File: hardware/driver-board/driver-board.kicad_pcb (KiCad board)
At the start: 4 copper layers, 111.8 x 83.8 mm, 0 parts

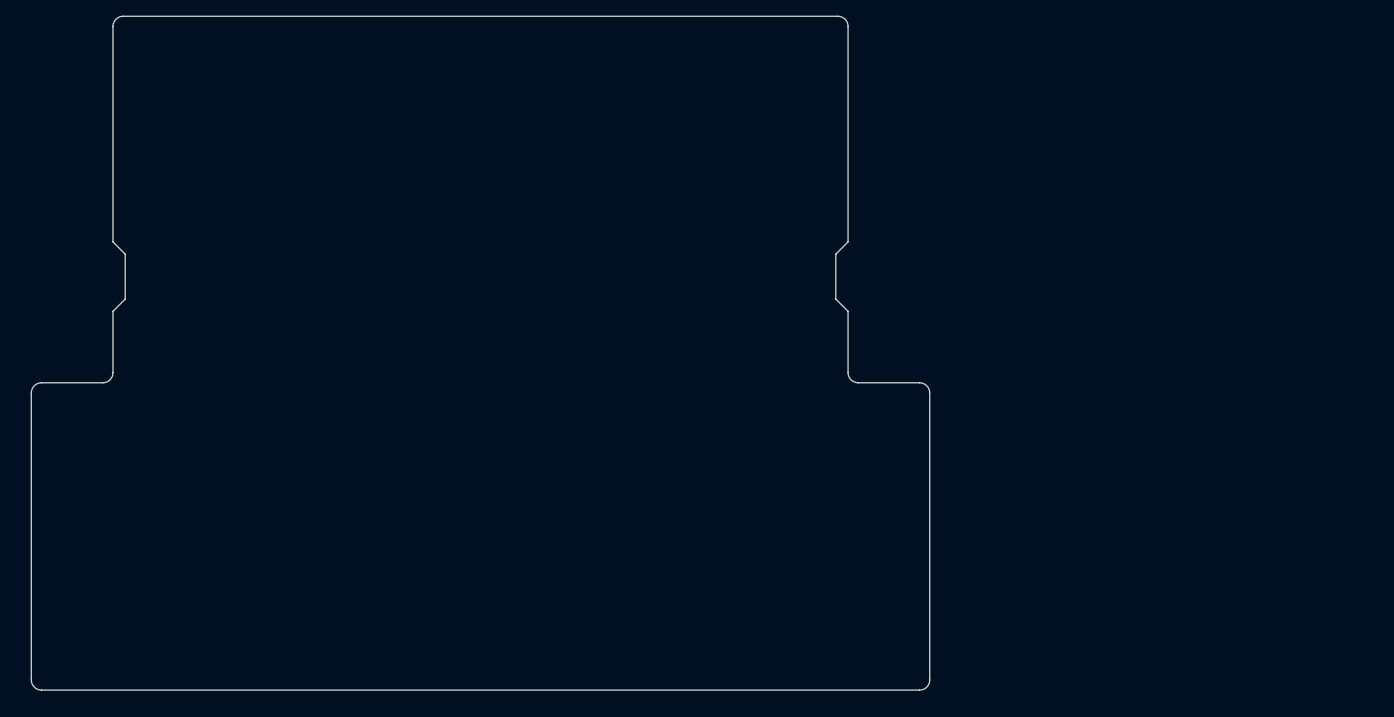
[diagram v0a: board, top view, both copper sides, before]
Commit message: Complete Romi-compatible board placement and power switching
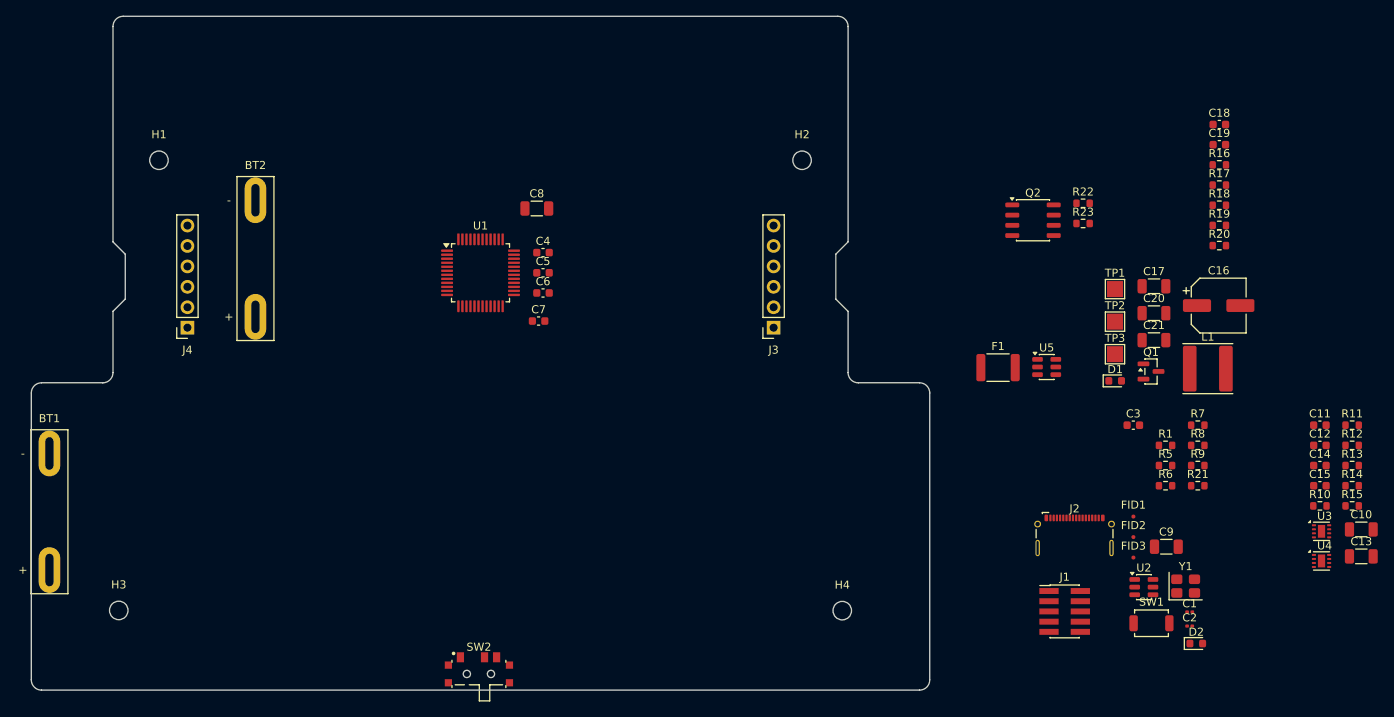
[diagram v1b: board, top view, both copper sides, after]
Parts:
- added BT1: BATT (4xAA), CustomParts:Romi_Chassis_BatteryContactPair_2Slot_14_50mm, F.Cu at (46.4, 119.7)
- added BT2: BATT (2xAA), CustomParts:Romi_Chassis_BatteryContactPair_2Slot_14_50mm, F.Cu at (72.0, 88.2)
- added C1: 10p, Capacitor_SMD:C_0201_0603Metric, F.Cu at (188.2, 132.2)
- added C10: 10u, Capacitor_SMD:C_1206_3216Metric, F.Cu at (209.6, 121.9)
- added C11: 100n, Capacitor_SMD:C_0603_1608Metric, F.Cu at (204.4, 109.0)
- added C12: 100n, Capacitor_SMD:C_0603_1608Metric, F.Cu at (204.4, 111.5)
- added C13: 10u, Capacitor_SMD:C_1206_3216Metric, F.Cu at (209.6, 125.3)
- added C14: 100n, Capacitor_SMD:C_0603_1608Metric, F.Cu at (204.4, 114.0)
- added C15: 100n, Capacitor_SMD:C_0603_1608Metric, F.Cu at (204.4, 116.5)
- added C16: 220u, Capacitor_SMD:CP_Elec_6.3x7.7, F.Cu at (191.8, 94.1)
- added C17: 10u, Capacitor_SMD:C_1206_3216Metric, F.Cu at (183.8, 91.7)
- added C18: 0.1u, Capacitor_SMD:C_0603_1608Metric, F.Cu at (191.9, 71.6)
- added C19: 0.1u, Capacitor_SMD:C_0603_1608Metric, F.Cu at (191.9, 74.1)
- added C2: 10p, Capacitor_SMD:C_0201_0603Metric, F.Cu at (188.2, 133.9)
- added C20: 22u, Capacitor_SMD:C_1206_3216Metric, F.Cu at (183.8, 95.0)
- added C21: 22u, Capacitor_SMD:C_1206_3216Metric, F.Cu at (183.8, 98.4)
- added C3: 100n, Capacitor_SMD:C_0603_1608Metric, F.Cu at (181.2, 109.0)
- added C4: 100n, Capacitor_SMD:C_0603_1608Metric, F.Cu at (107.8, 87.5)
- added C5: 100n, Capacitor_SMD:C_0603_1608Metric, F.Cu at (107.8, 90.0)
- added C6: 100n, Capacitor_SMD:C_0603_1608Metric, F.Cu at (107.8, 92.5)
- added C7: 100n, Capacitor_SMD:C_0603_1608Metric, F.Cu at (107.2, 96.0)
- added C8: 10u, Capacitor_SMD:C_1206_3216Metric, F.Cu at (107.0, 82.0)
- added C9: 10u, Capacitor_SMD:C_1206_3216Metric, F.Cu at (185.3, 124.1)
- added D1: PWR_ON_LED, LED_SMD:LED_0603_1608Metric, F.Cu at (178.9, 103.4)
- added D2: STATUS, LED_SMD:LED_0603_1608Metric, F.Cu at (189.0, 136.1)
- added F1: PTC_2.6A_16V, Fuse:Fuse_1812_4532Metric, F.Cu at (164.4, 101.8)
- added FID1: Fiducial, Fiducial:Fiducial_0.5mm_Mask1mm, F.Cu at (181.2, 120.3)
- added FID2: Fiducial, Fiducial:Fiducial_0.5mm_Mask1mm, F.Cu at (181.2, 122.9)
- added FID3: Fiducial, Fiducial:Fiducial_0.5mm_Mask1mm, F.Cu at (181.2, 125.4)
- added H1: MountingHole, CustomParts:MountingHole_2.3mm_2-56, F.Cu at (60.0, 76.0)
- added H2: MountingHole, CustomParts:MountingHole_2.3mm_2-56, F.Cu at (140.0, 76.0)
- added H3: MountingHole, CustomParts:MountingHole_2.3mm_2-56, F.Cu at (55.0, 132.0)
- added H4: MountingHole, CustomParts:MountingHole_2.3mm_2-56, F.Cu at (145.0, 132.0)
- added J1: Conn_ARM_JTAG_SWD_10, Connector_PinHeader_1.27mm:PinHeader_2x05_P1.27mm_Vertical_SMD, F.Cu at (172.7, 132.1)
- added J2: USB_C_Receptacle_USB2.0_16P, Connector_USB:USB_C_Receptacle_G-Switch_GT-USB-7025, F.Cu at (173.9, 123.9)
- added J3: CONN_MOTOR_R, Connector_PinSocket_2.54mm:PinSocket_1x06_P2.54mm_Vertical, F.Cu at (136.5, 96.8)
- added J4: CONN_MOTOR_L, Connector_PinSocket_2.54mm:PinSocket_1x06_P2.54mm_Vertical, F.Cu at (63.5, 96.8)
- added L1: 5.6u, Inductor_SMD:L_Sunlord_SWPA6045S, F.Cu at (190.5, 101.9)
- added Q1: AO3401A, Package_TO_SOT_SMD:SOT-23, F.Cu at (183.4, 102.3)
- added Q2: AO4407A, CustomParts:AO4407A_SO-8_GSD, F.Cu at (168.7, 83.5)
- added R1: 10k, Resistor_SMD:R_0603_1608Metric, F.Cu at (185.2, 111.5)
- added R10: 10k, Resistor_SMD:R_0603_1608Metric, F.Cu at (204.4, 119.0)
- added R11: 10k, Resistor_SMD:R_0603_1608Metric, F.Cu at (208.4, 109.0)
- added R12: 100k, Resistor_SMD:R_0603_1608Metric, F.Cu at (208.4, 111.5)
- added R13: 100k, Resistor_SMD:R_0603_1608Metric, F.Cu at (208.4, 114.0)
- added R14: 10k, Resistor_SMD:R_0603_1608Metric, F.Cu at (208.4, 116.5)
- added R15: 10k, Resistor_SMD:R_0603_1608Metric, F.Cu at (208.4, 119.0)
- added R16: 100k, Resistor_SMD:R_0603_1608Metric, F.Cu at (191.9, 76.6)
- added R17: 33k, Resistor_SMD:R_0603_1608Metric, F.Cu at (191.9, 79.1)
- added R18: 100k, Resistor_SMD:R_0603_1608Metric, F.Cu at (191.9, 81.6)
- added R19: 22.1k, Resistor_SMD:R_0603_1608Metric, F.Cu at (191.9, 84.1)
- added R20: 1k, Resistor_SMD:R_0603_1608Metric, F.Cu at (191.9, 86.6)
- added R21: 1k, Resistor_SMD:R_0603_1608Metric, F.Cu at (189.2, 116.5)
- added R22: 100k, Resistor_SMD:R_0603_1608Metric, F.Cu at (175.0, 81.4)
- added R23: 1k, Resistor_SMD:R_0603_1608Metric, F.Cu at (175.0, 83.9)
- added R5: 1k5, Resistor_SMD:R_0603_1608Metric, F.Cu at (185.2, 114.0)
- added R6: 5k1, Resistor_SMD:R_0603_1608Metric, F.Cu at (185.2, 116.5)
- added R7: 5k1, Resistor_SMD:R_0603_1608Metric, F.Cu at (189.2, 109.0)
- added R8: 22, Resistor_SMD:R_0603_1608Metric, F.Cu at (189.2, 111.5)
- added R9: 22, Resistor_SMD:R_0603_1608Metric, F.Cu at (189.2, 114.0)
- added SW1: SW_Push, Button_Switch_SMD:SW_SPST_TS-1088-xR020, F.Cu at (183.5, 133.6)
- added SW2: SK-3296S-01-L2, CustomParts:SW_SPDT_RightAngle_XKB_SK-3296S-01-L2, F.Cu at (99.8, 139.9)
- added TP1: TP_3V3, TestPoint:TestPoint_Pad_2.0x2.0mm, F.Cu at (178.9, 92.0)
- added TP2: TP_GND, TestPoint:TestPoint_Pad_2.0x2.0mm, F.Cu at (178.9, 96.1)
- added TP3: TV_BAT, TestPoint:TestPoint_Pad_2.0x2.0mm, F.Cu at (178.9, 100.1)
- added U1: STM32F103CBT6, Package_QFP:LQFP-48_7x7mm_P0.5mm, F.Cu at (100.0, 90.0)
- added U2: USBLC6-2SC6, Package_TO_SOT_SMD:SOT-23-6, F.Cu at (182.5, 129.1)
- added U3: DRV8838, Package_SON:WSON-8-1EP_2x2mm_P0.5mm_EP0.9x1.6mm, F.Cu at (204.6, 122.2)
- added U4: DRV8838, Package_SON:WSON-8-1EP_2x2mm_P0.5mm_EP0.9x1.6mm, F.Cu at (204.6, 125.8)
- added U5: LMR51430XDDCR, Package_TO_SOT_SMD:SOT-23-6, F.Cu at (170.4, 101.7)
- added Y1: 16Mhz, Crystal:Crystal_SMD_3225-4Pin_3.2x2.5mm, F.Cu at (187.7, 129.0)
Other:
- board text added: "BAT1+ ROMI BATTERY SLOT"
- board text added: "BAT1- ROMI BATTERY SLOT"
- board text added: "BAT2+ ROMI BATTERY SLOT"
- board text added: "BAT2- ROMI BATTERY SLOT"

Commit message: Review and harden Rev A driver board
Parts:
- removed FID1, FID2, FID3: Fiducial, Fiducial:Fiducial_0.5mm_Mask1mm
- L1: footprint Inductor_SMD:L_Sunlord_SWPA6045S -> Inductor_SMD:L_APV_ANR8065
- moved C17 158.9 mm to (28.6, 125.8)
- moved C20 158.9 mm to (28.6, 129.1)
- moved C21 158.9 mm to (28.6, 132.4)
- moved R19 158.9 mm to (36.7, 118.2)
- moved TP1 158.9 mm to (23.7, 126.1)
- moved C19 125.6 mm to (78.0, 127.0), turned to 180 degrees
- moved Q1 124.8 mm to (60.0, 121.0), turned to 180 degrees
- moved C18 123.4 mm to (78.0, 119.0), turned to 180 degrees
- moved R18 118.8 mm to (81.0, 124.2), turned to -90 degrees
- moved C16 114.6 mm to (79.0, 114.0), turned to 180 degrees
- moved F1 112.0 mm to (54.0, 121.0)
- moved L1 98.2 mm to (94.0, 120.0), turned to 90 degrees
- moved U5 95.1 mm to (78.0, 124.0)
- moved J2 75.4 mm to (100.0, 139.0)
- moved SW2 34.3 mm to (66.5, 148.0)
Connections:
- net Net-(Q1-D) renamed /Power/VBAT_FUSED
- R21 pad 1: Net-(D2-K) -> +3V3
- R21 pad 2: GND -> Net-(D2-A)
- U1 pad 2: Net-(D2-A) -> Net-(D2-K)

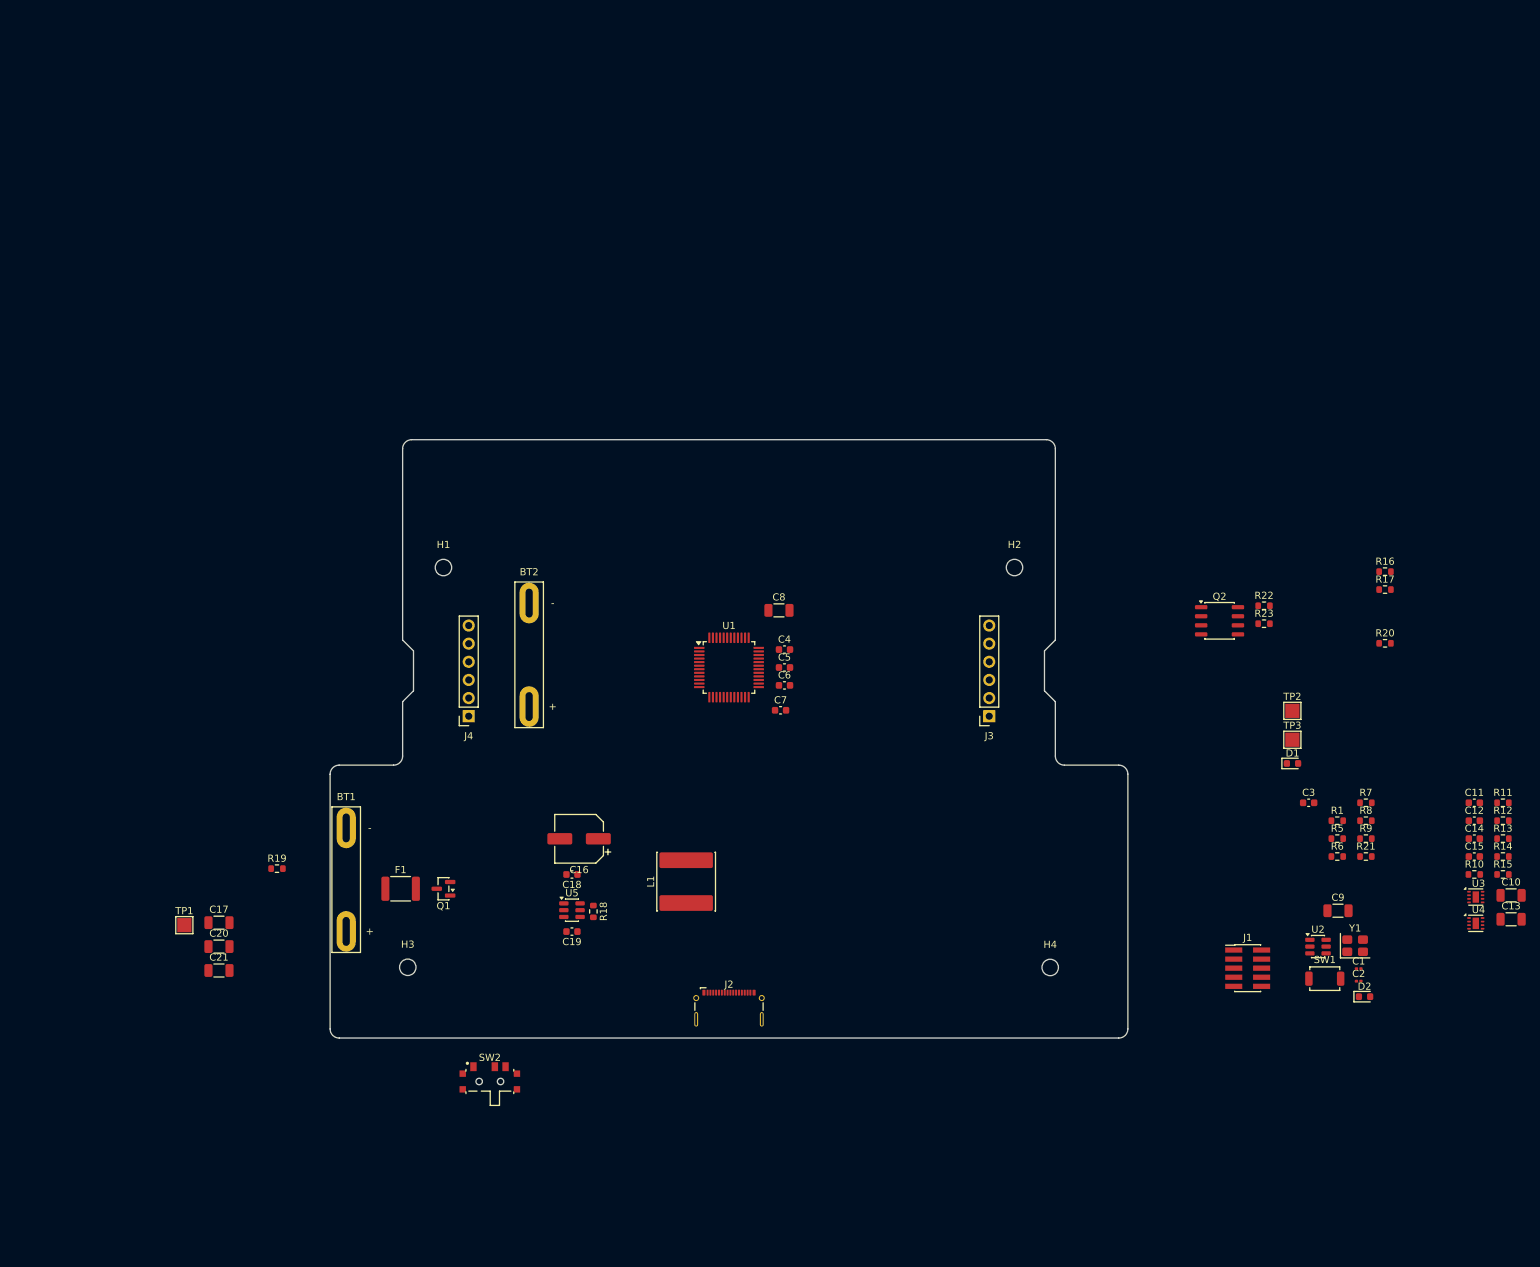
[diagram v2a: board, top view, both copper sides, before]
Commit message: Refine driver board placement and capacitor footprints
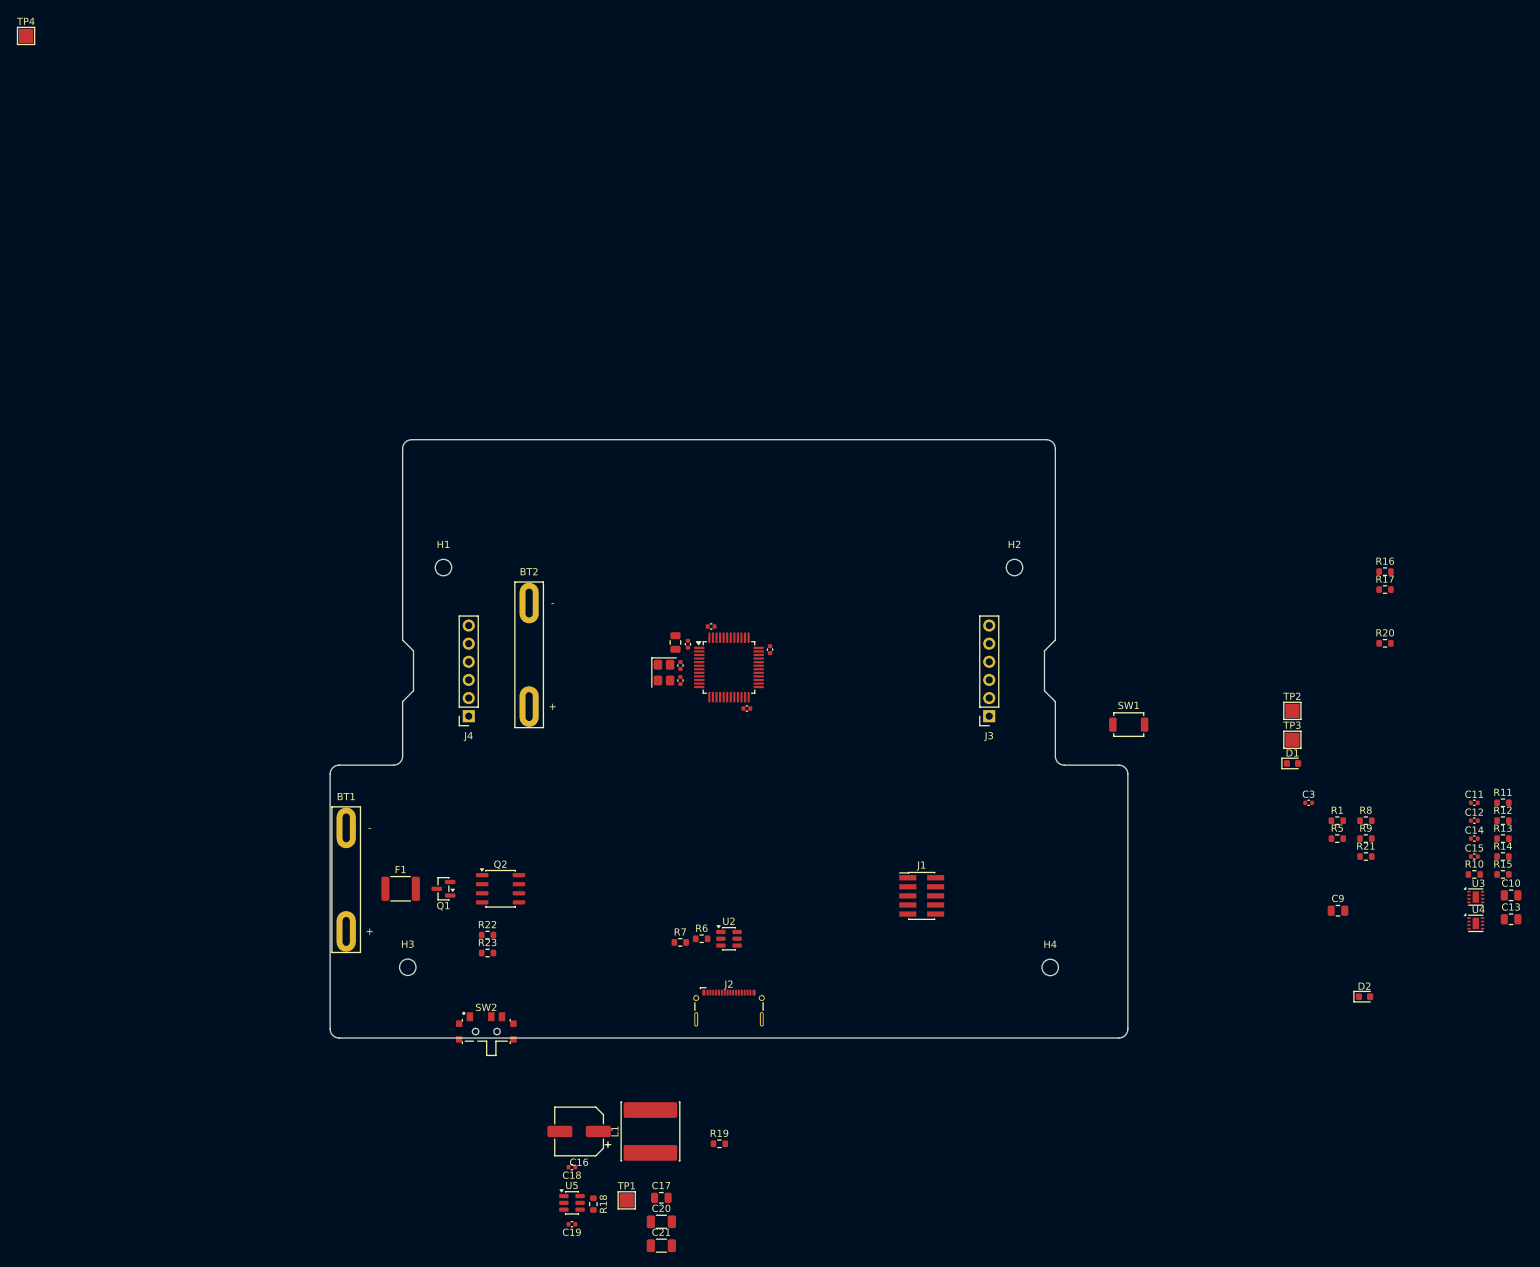
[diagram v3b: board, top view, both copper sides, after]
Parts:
- added TP4: TP_BAT_SW, TestPoint:TestPoint_Pad_2.0x2.0mm, F.Cu at (1.52, 1.52)
- C1, C2: footprint Capacitor_SMD:C_0201_0603Metric -> Capacitor_SMD:C_0402_1005Metric
- C10, C13, C17, C8, C9: footprint Capacitor_SMD:C_1206_3216Metric -> Capacitor_SMD:C_0805_2012Metric
- C11, C12, C14, C15, C3, C4, C5, C6, C7: footprint Capacitor_SMD:C_0603_1608Metric -> Capacitor_SMD:C_0402_1005Metric
- C18, C19: value 0.1u -> 100n; footprint Capacitor_SMD:C_0603_1608Metric -> Capacitor_SMD:C_0402_1005Metric
- TP3: value TV_BAT -> TP_BAT
- moved R22 118.2 mm to (66.2, 127.5)
- moved R23 118.2 mm to (66.2, 130.0)
- moved Q2 107.5 mm to (68.0, 121.0)
- moved Y1 104.1 mm to (90.9, 90.7), turned to -90 degrees
- moved C1 104.1 mm to (93.2, 89.7), turned to -90 degrees
- moved C2 103.9 mm to (93.2, 91.8), turned to 90 degrees
- moved R7 98.0 mm to (93.2, 128.5)
- moved R6 89.8 mm to (96.2, 128.0)
- moved U2 82.5 mm to (100.0, 128.0)
- moved C17 73.0 mm to (90.5, 164.3)
- moved C20 73.0 mm to (90.5, 167.7)
- moved C21 73.0 mm to (90.5, 171.0)
- moved R19 73.0 mm to (98.7, 156.7)
- moved TP1 73.0 mm to (85.7, 164.7)
- moved J1 46.8 mm to (127.0, 122.0)
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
